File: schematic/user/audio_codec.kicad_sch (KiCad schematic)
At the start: 23 parts, among them U4 TLV320AIC3254IRHBR

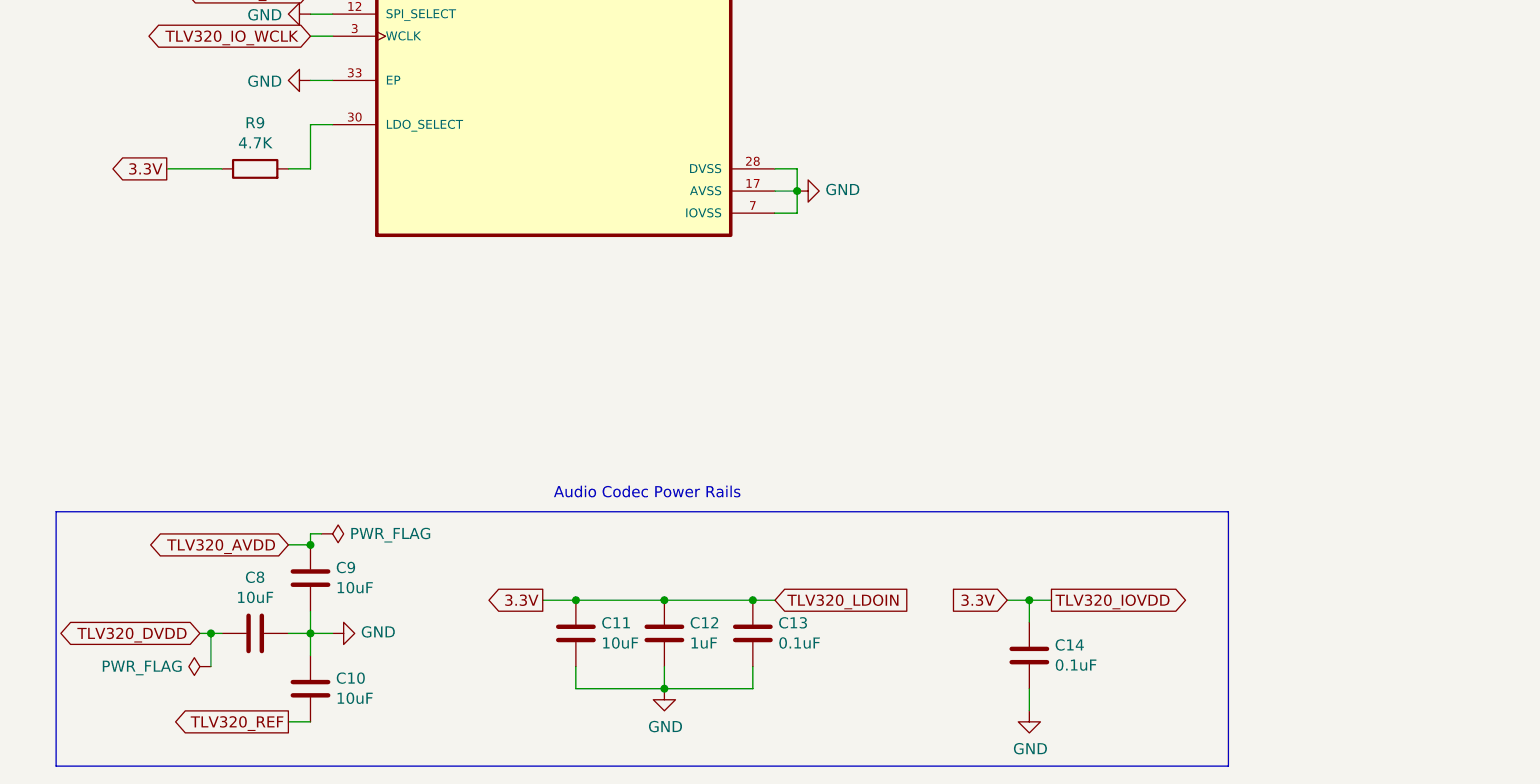
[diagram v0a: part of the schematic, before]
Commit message: v0.4 board: add MOSFET power control for TLV320 and other peripherals
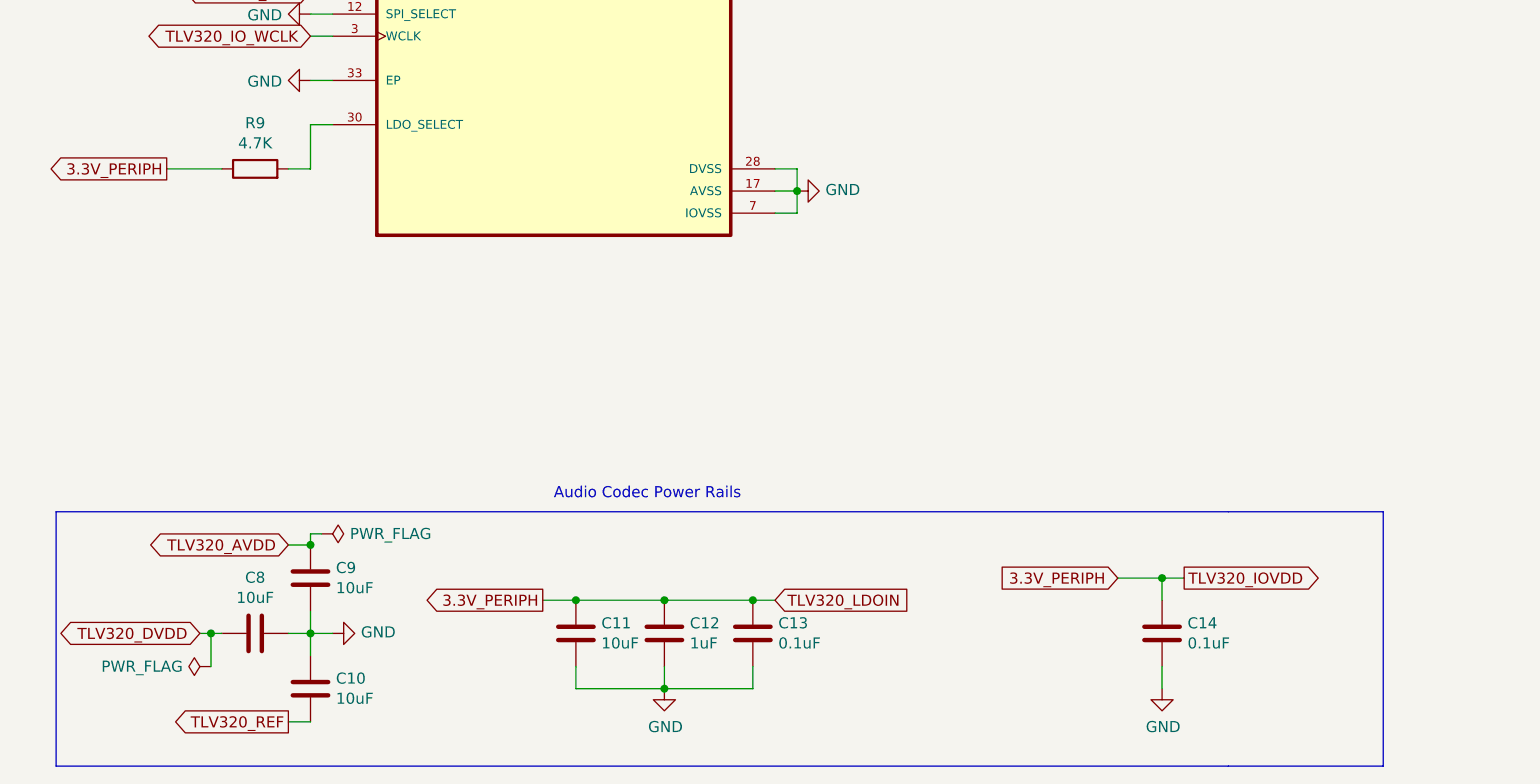
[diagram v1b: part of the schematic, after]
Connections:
- net 3.3V: no longer C11.1, C12.1, C13.1, C14.1, R9.1, U4.26 (LDOIN), U4.6 (OVIDD)
- new net 3.3V_PERIPH: C11.1, C12.1, C13.1, C14.1, R9.1, U4.26 (LDOIN), U4.6 (OVIDD)
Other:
- moved on the sheet: C14
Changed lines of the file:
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@@
   (junction (at 224.79 132.08) (diameter 0) (color 0 0 0 0)
   )
-  (junction (at 133.35 173.99) (diameter 0) (color 0 0 0 0)
+  (junction (at 148.59 171.45) (diameter 0) (color 0 0 0 0)
   )
   (junction (at 50.8 167.64) (diameter 0) (color 0 0 0 0)
@@
     (stroke (width 0) (type default) (color 0 0 0 0))
   )
-  (wire (pts (xy 133.35 173.99) (xy 135.89 173.99))
+  (wire (pts (xy 148.59 171.45) (xy 151.13 171.45))
     (stroke (width 0) (type default) (color 0 0 0 0))
   )
@@
     (stroke (width 0) (type default) (color 0 0 0 0))
   )
+  (polyline (pts (xy 156.21 193.04) (xy 173.99 193.04))
+    (stroke (width 0) (type default) (color 0 0 0 0))
+  )
   (wire (pts (xy 53.34 83.82) (xy 49.53 83.82))
     (stroke (width 0) (type default) (color 0 0 0 0))
@@
     (stroke (width 0) (type default) (color 0 0 0 0))
   )
+  (polyline (pts (xy 156.21 163.83) (xy 173.99 163.83))
+    (stroke (width 0) (type default) (color 0 0 0 0))
+  )
   (wire (pts (xy 39.37 177.8) (xy 38.1 177.8))
     (stroke (width 0) (type default) (color 0 0 0 0))
@@
     (stroke (width 0) (type default) (color 0 0 0 0))
   )
-  (wire (pts (xy 130.81 173.99) (xy 133.35 173.99))
-    (stroke (width 0) (type default) (color 0 0 0 0))
-  )
-  (wire (pts (xy 133.35 184.15) (xy 133.35 186.69))
+  (wire (pts (xy 143.51 171.45) (xy 148.59 171.45))
+    (stroke (width 0) (type default) (color 0 0 0 0))
+  )
+  (wire (pts (xy 148.59 181.61) (xy 148.59 184.15))
     (stroke (width 0) (type default) (color 0 0 0 0))
   )
@@
     (stroke (width 0) (type default) (color 0 0 0 0))
   )
-  (wire (pts (xy 133.35 176.53) (xy 133.35 173.99))
-    (stroke (width 0) (type default) (color 0 0 0 0))
-  )
-  (polyline (pts (xy 156.21 163.83) (xy 156.21 193.04))
+  (wire (pts (xy 148.59 173.99) (xy 148.59 171.45))
+    (stroke (width 0) (type default) (color 0 0 0 0))
+  )
+  (polyline (pts (xy 173.99 163.83) (xy 173.99 193.04))
     (stroke (width 0) (type default) (color 0 0 0 0))
   )
@@
     )
   )
-  (global_label "TLV320_IOVDD" (shape output) (at 135.89 173.99 0) (fields_autoplaced)
-    (effects (font (size 1.27 1.27)) (justify left))
-    (property "Intersheet References" "${INTERSHEET_REFS}" (id 0) (at -2.54 7.62 0)
+  (global_label "TLV320_IOVDD" (shape output) (at 151.13 171.45 0) (fields_autoplaced)
+    (effects (font (size 1.27 1.27)) (justify left))
+    (property "Intersheet References" "${INTERSHEET_REFS}" (id 0) (at 12.7 5.08 0)
       (effects (font (size 1.27 1.27)) hide)
     )
@@
     )
   )
-  (global_label "3.3V" (shape output) (at 34.29 124.46 180) (fields_autoplaced)
-    (effects (font (size 1.27 1.27)) (justify right))
-    (property "Intersheet References" "${INTERSHEET_REFS}" (id 0) (at -2.54 7.62 0)
-      (effects (font (size 1.27 1.27)) hide)
+  (global_label "3.3V_PERIPH" (shape output) (at 34.29 124.46 180) (fields_autoplaced)
+    (effects (font (size 1.27 1.27)) (justify right))
+    (property "Intersheet References" "${INTERSHEET_REFS}" (id 0) (at 19.9026 124.3806 0)
+      (effects (font (size 1.27 1.27)) (justify right) hide)
     )
   )
@@
     )
   )
-  (global_label "3.3V" (shape output) (at 77.47 173.99 180) (fields_autoplaced)
-    (effects (font (size 1.27 1.27)) (justify right))
-    (property "Intersheet References" "${INTERSHEET_REFS}" (id 0) (at -2.54 7.62 0)
-      (effects (font (size 1.27 1.27)) hide)
+  (global_label "3.3V_PERIPH" (shape output) (at 77.47 173.99 180) (fields_autoplaced)
+    (effects (font (size 1.27 1.27)) (justify right))
+    (property "Intersheet References" "${INTERSHEET_REFS}" (id 0) (at 63.0826 173.9106 0)
+      (effects (font (size 1.27 1.27)) (justify right) hide)
     )
   )
@@
     )
   )
-  (global_label "3.3V" (shape input) (at 130.81 173.99 180) (fields_autoplaced)
-    (effects (font (size 1.27 1.27)) (justify right))
-    (property "Intersheet References" "${INTERSHEET_REFS}" (id 0) (at -2.54 7.62 0)
-      (effects (font (size 1.27 1.27)) hide)
+  (global_label "3.3V_PERIPH" (shape input) (at 143.51 171.45 180) (fields_autoplaced)
+    (effects (font (size 1.27 1.27)) (justify right))
+    (property "Intersheet References" "${INTERSHEET_REFS}" (id 0) (at 129.1226 171.3706 0)
+      (effects (font (size 1.27 1.27)) (justify right) hide)
     )
   )
@@
     (pin "2")
   )
-  (symbol (lib_id "Device:C") (at 133.35 180.34 0) (unit 1)
-    (in_bom yes) (on_board yes)
-    (property "Reference" "C14" (id 0) (at 136.271 179.1716 0)
-      (effects (font (size 1.27 1.27)) (justify left))
-    )
-    (property "Value" "0.1uF" (id 1) (at 136.271 181.483 0)
-      (effects (font (size 1.27 1.27)) (justify left))
-    )
-    (property "Footprint" "Capacitor_SMD:C_0402_1005Metric" (id 2) (at 134.3152 184.15 0)
-      (effects (font (size 1.27 1.27)) hide)
-    )
-    (property "Datasheet" "https://datasheet.lcsc.com/lcsc/1810191219_Samsung-Electro-Mechanics-CL05B104KO5NNNC_C1525.pdf" (id 3) (at 133.35 180.34 0)
-      (effects (font (size 1.27 1.27)) hide)
-    )
-    (property "LCSC" "C1525" (id 4) (at 133.35 180.34 0)
+  (symbol (lib_id "Device:C") (at 148.59 177.8 0) (unit 1)
+    (in_bom yes) (on_board yes)
+    (property "Reference" "C14" (id 0) (at 151.511 176.6316 0)
+      (effects (font (size 1.27 1.27)) (justify left))
+    )
+    (property "Value" "0.1uF" (id 1) (at 151.511 178.943 0)
+      (effects (font (size 1.27 1.27)) (justify left))
+    )
+    (property "Footprint" "Capacitor_SMD:C_0402_1005Metric" (id 2) (at 149.5552 181.61 0)
+      (effects (font (size 1.27 1.27)) hide)
+    )
+    (property "Datasheet" "https://datasheet.lcsc.com/lcsc/1810191219_Samsung-Electro-Mechanics-CL05B104KO5NNNC_C1525.pdf" (id 3) (at 148.59 177.8 0)
+      (effects (font (size 1.27 1.27)) hide)
+    )
+    (property "LCSC" "C1525" (id 4) (at 148.59 177.8 0)
       (effects (font (size 1.27 1.27)) hide)
     )
@@
     (pin "2")
   )
-  (symbol (lib_id "power:GND") (at 133.35 186.69 0) (unit 1)
-    (in_bom yes) (on_board yes)
-    (property "Reference" "#PWR018" (id 0) (at 133.35 193.04 0)
-      (effects (font (size 1.27 1.27)) hide)
-    )
-    (property "Value" "GND" (id 1) (at 133.477 191.0842 0))
-    (property "Footprint" "" (id 2) (at 133.35 186.69 0)
-      (effects (font (size 1.27 1.27)) hide)
-    )
-    (property "Datasheet" "" (id 3) (at 133.35 186.69 0)
-      (effects (font (size 1.27 1.27)) hide)
-    )
+  (symbol (lib_id "power:GND") (at 148.59 184.15 0) (unit 1)
+    (in_bom yes) (on_board yes)
+    (property "Reference" "#PWR018" (id 0) (at 148.59 190.5 0)
+      (effects (font (size 1.27 1.27)) hide)
+    )
+    (property "Value" "GND" (id 1) (at 148.717 188.5442 0))
+    (property "Footprint" "" (id 2) (at 148.59 184.15 0)
+      (effects (font (size 1.27 1.27)) hide)
+    )
+    (property "Datasheet" "" (id 3) (at 148.59 184.15 0)
+      (effects (font (size 1.27 1.27)) hide)
+    )

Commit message: v0.4 board: substitute JLCPCB basic parts where possible ($3/component savings).
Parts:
- C15, C18: LCSC C387962 -> C47339
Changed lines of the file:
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@@
       (effects (font (size 1.27 1.27)) hide)
     )
-    (property "Datasheet" "https://datasheet.lcsc.com/lcsc/1912111437_Walsin-Tech-Corp-0402X474K250CT_C387962.pdf" (id 3) (at 156.21 68.58 0)
+    (property "Datasheet" "https://datasheet.lcsc.com/lcsc/1810191214_Samsung-Electro-Mechanics-CL05A474KP5NNNC-_C47339.pdf" (id 3) (at 156.21 68.58 0)
       (effects (font (size 1.27 1.27)) hide)
     )
-    (property "LCSC" "C387962" (id 4) (at 156.21 68.58 0)
+    (property "LCSC" "C47339" (id 4) (at 156.21 68.58 0)
       (effects (font (size 1.27 1.27)) hide)
     )
@@
       (effects (font (size 1.27 1.27)) hide)
     )
-    (property "Datasheet" "https://datasheet.lcsc.com/lcsc/1912111437_Walsin-Tech-Corp-0402X474K250CT_C387962.pdf" (id 3) (at 255.27 34.29 0)
+    (property "Datasheet" "https://datasheet.lcsc.com/lcsc/1810191214_Samsung-Electro-Mechanics-CL05A474KP5NNNC-_C47339.pdf" (id 3) (at 255.27 34.29 0)
       (effects (font (size 1.27 1.27)) hide)
     )
-    (property "LCSC" "C387962" (id 4) (at 255.27 34.29 0)
+    (property "LCSC" "C47339" (id 4) (at 255.27 34.29 0)
       (effects (font (size 1.27 1.27)) hide)
     )

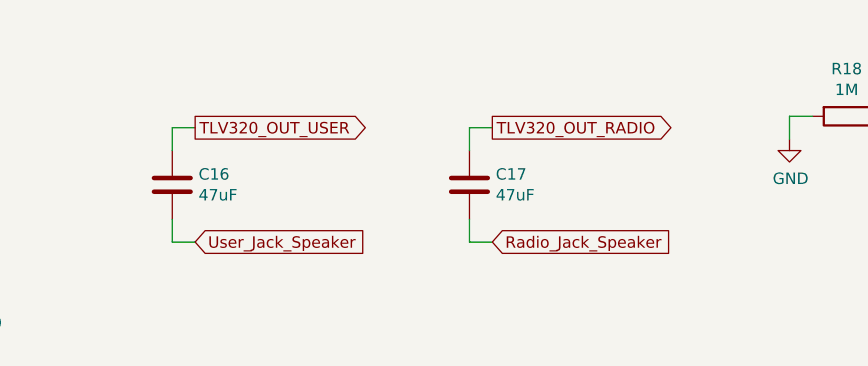
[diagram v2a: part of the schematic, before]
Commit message: v0.4 board: increase power trace width, reposition decoupling caps, add missing depop resistors
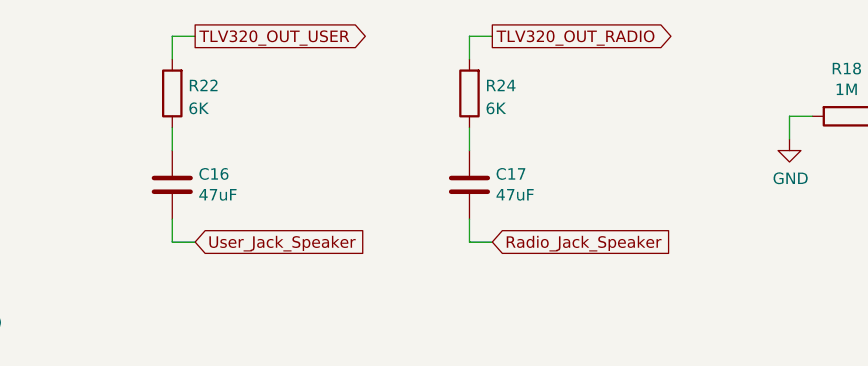
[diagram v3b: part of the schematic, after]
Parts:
- added R22, R24: 6K, Resistor_SMD:R_0402_1005Metric, symbol Device:R
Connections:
- net TLV320_OUT_RADIO: now also R24.2; no longer C17.1
- net TLV320_OUT_USER: now also R22.2; no longer C16.1
- new net: C16.1, R22.1
- new net: C17.1, R24.1

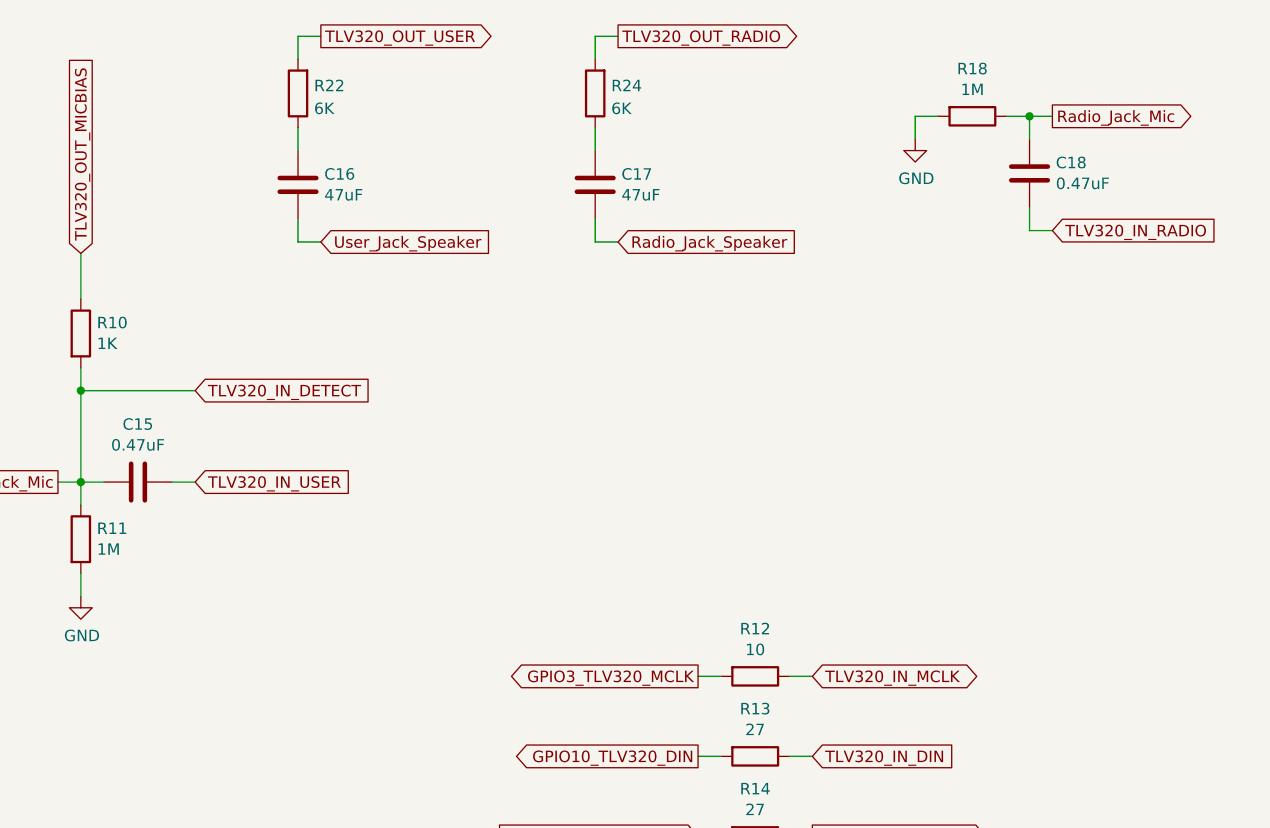
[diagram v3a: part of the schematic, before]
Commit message: v0.4 board: more tweaks to circuit traces and new components
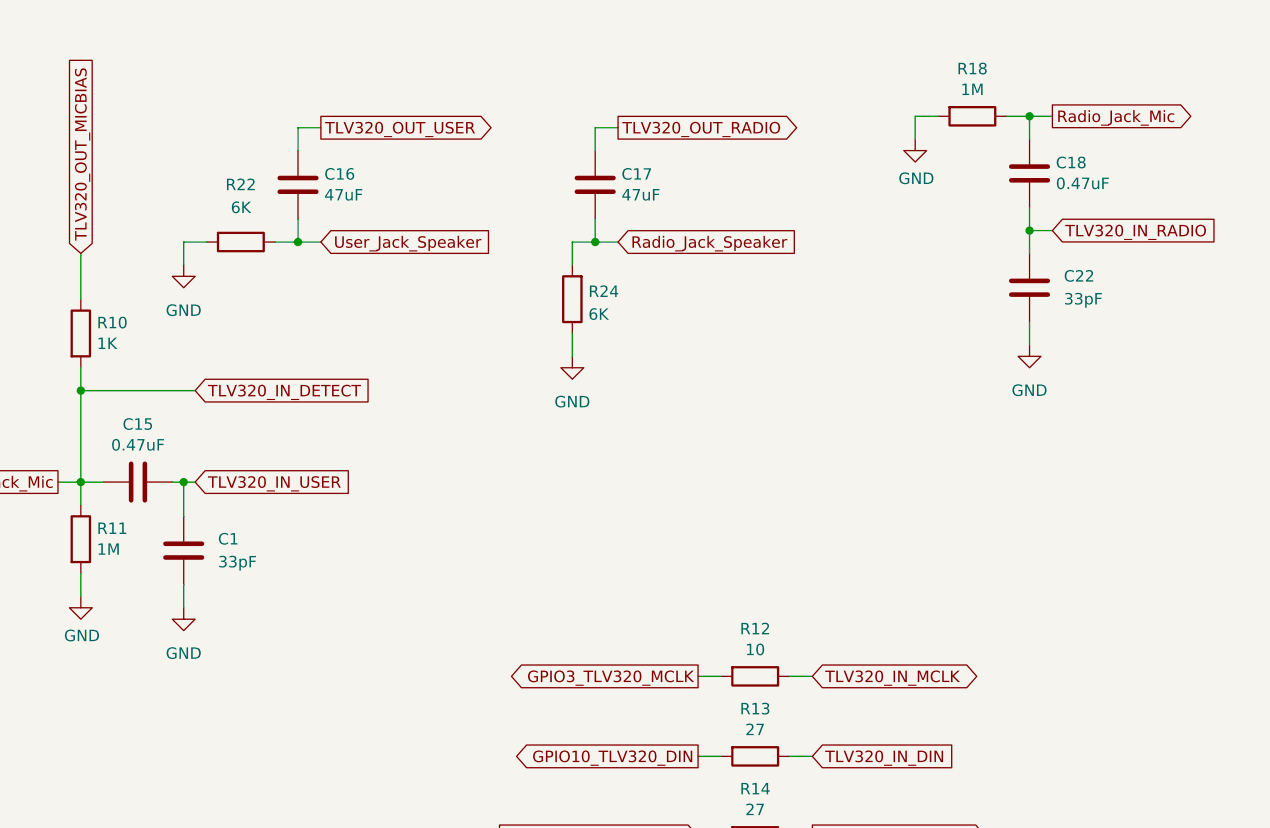
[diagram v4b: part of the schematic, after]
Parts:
- added C1, C22: 33pF, Capacitor_SMD:C_0402_1005Metric, symbol Device:C
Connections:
- net GND: now also R22.2, R24.1, C1.2, C22.2
- net Radio_Jack_Speaker: now also R24.2
- net TLV320_IN_RADIO: now also C22.1
- net TLV320_IN_USER: now also C1.1
- net TLV320_OUT_RADIO: now also C17.1; no longer R24.2
- net TLV320_OUT_USER: now also C16.1; no longer R22.2
- net User_Jack_Speaker: now also R22.1
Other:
- moved on the sheet: R22, R24
